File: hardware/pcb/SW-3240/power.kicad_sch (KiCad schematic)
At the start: 59 parts, among them SW1 PWR_SW, U10 LMR14050, U11 NCP1117-3.3, U8 TPS54231, U9 LM2941

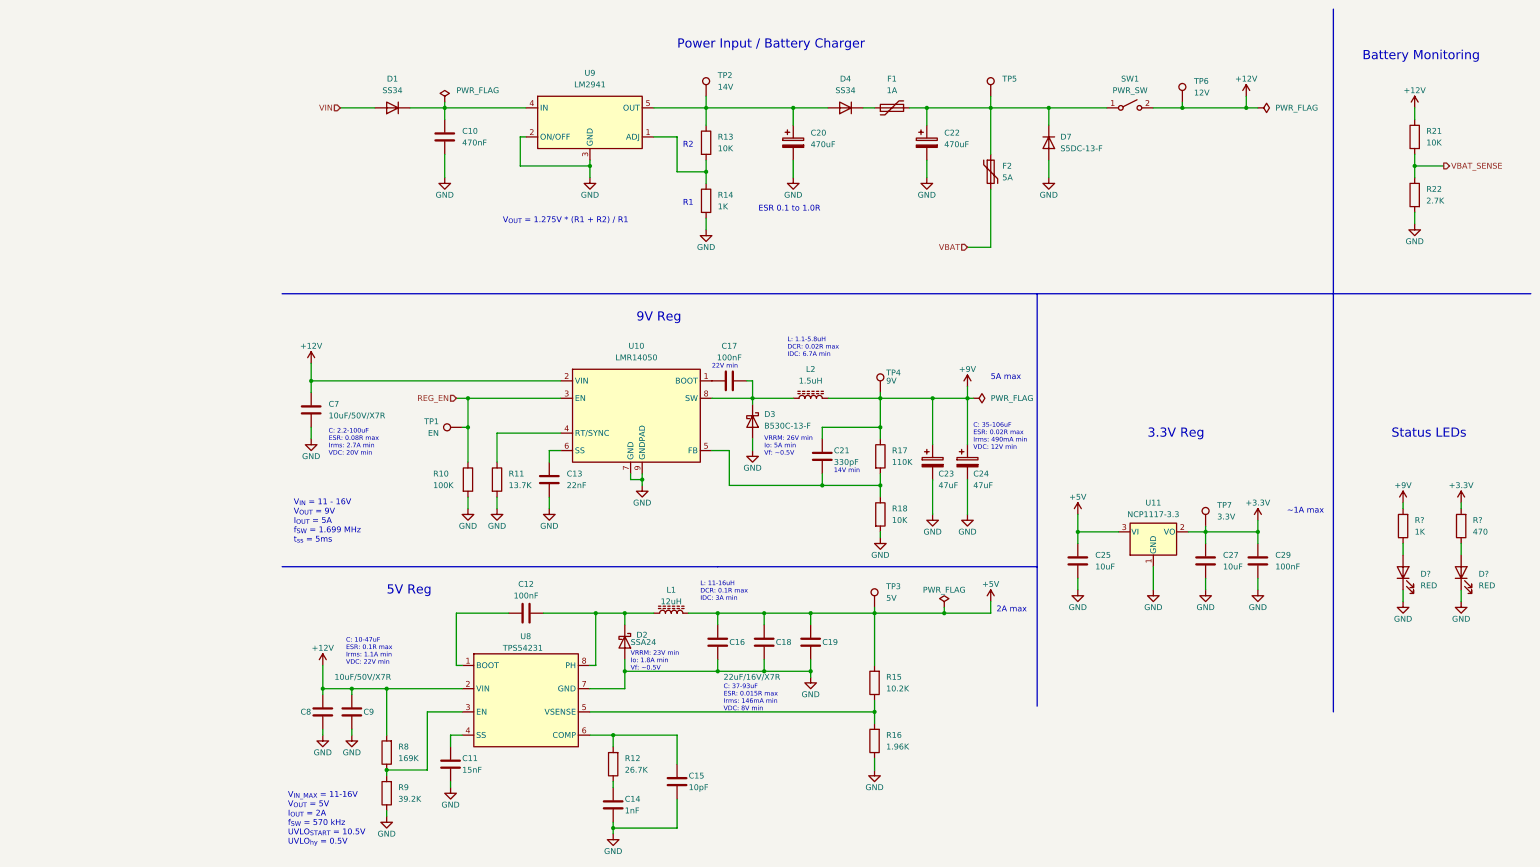
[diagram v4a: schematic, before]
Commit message: use atmega328pb for main board
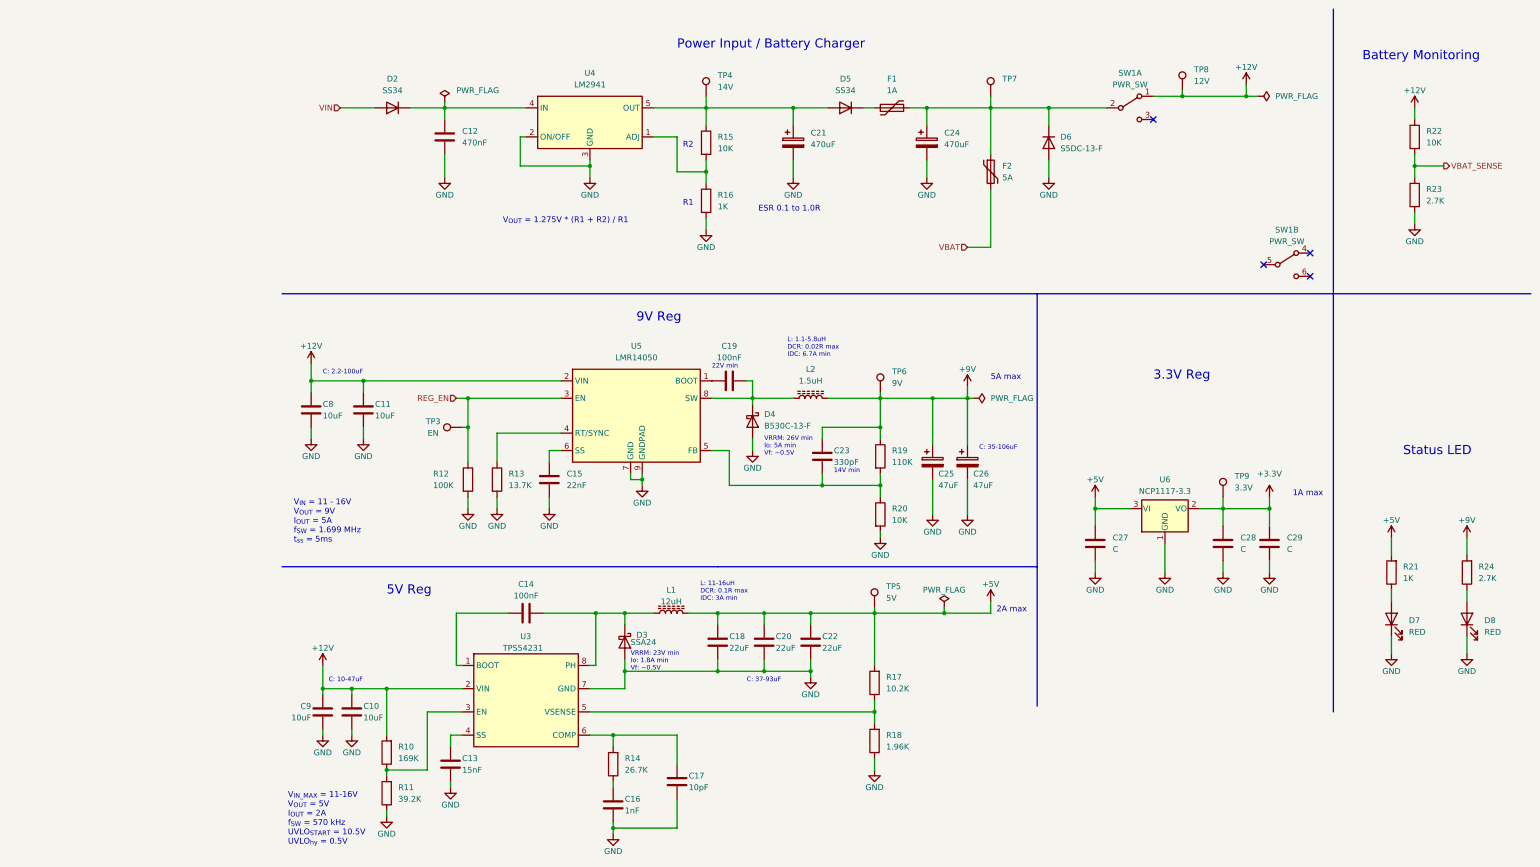
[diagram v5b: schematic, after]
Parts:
- removed C25: 10uF, Capacitor_SMD:C_0603_1608Metric, symbol Device:C
- removed D?: RED, LED_SMD:LED_0805_2012Metric, symbol Device:LED
- removed R?: 470, Resistor_SMD:R_0603_1608Metric, symbol Device:R
- removed SW1: PWR_SW, Button_Switch_THT:SW_E-Switch_EG2219_DPDT_Angled, symbol Switch:SW_SPST
- removed TP7: 3.3V, TestPoint:TestPoint_THTPad_D2.0mm_Drill1.0mm, symbol Connector:TestPoint
- removed U11: NCP1117-3.3, Package_TO_SOT_SMD:SOT-223-3_TabPin2, symbol Regulator_Linear:NCP1117-3.3_SOT223
- added C11: 10uF, Capacitor_SMD:C_1210_3225Metric, symbol Device:C
- added C28: C, Capacitor_SMD:C_0603_1608Metric, symbol Device:C
- added D7: RED, LED_SMD:LED_0603_1608Metric, symbol Device:LED
- added R21: 1K, Resistor_SMD:R_0603_1608Metric, symbol Device:R
- added SW1: PWR_SW, Button_Switch_THT:SW_E-Switch_EG2219_DPDT_Angled, symbol Switch:SW_DPDT_x2
- added TP9: 3.3V, TestPoint:TestPoint_Pad_D1.5mm, symbol Connector:TestPoint
- added U6: NCP1117-3.3, Package_TO_SOT_SMD:SOT-223-3_TabPin2, symbol Regulator_Linear:NCP1117-3.3_SOT223
- C10: renamed from C9; value 10uF/50V/X7R -> 10uF
- C18: renamed from C16; value 22uF/16V/X7R -> 22uF
- C20: renamed from C18; value 22uF/16V/X7R -> 22uF
- C22: renamed from C19; value 22uF/16V/X7R -> 22uF
- C25: renamed from C23; footprint Capacitor_SMD:CP_Elec_5x4.4 -> Capacitor_SMD:C_Elec_6.3x5.8; LCSC (none) -> C2162033; MOUSER (none) -> 710-875105445006; MPN 16SVPG47M -> 875105445006
- C26: renamed from C24; footprint Capacitor_SMD:CP_Elec_5x4.4 -> Capacitor_SMD:C_Elec_6.3x5.8; LCSC (none) -> C2162033; MOUSER (none) -> 710-875105445006; MPN 16SVPG47M -> 875105445006
- C27: value 10uF -> C
- C29: value 100nF -> C
- C8: renamed from C7; value 10uF/50V/X7R -> 10uF
- C9: renamed from C8; value 10uF/50V/X7R -> 10uF
- D3: renamed from D2; value SSA24 -> SSA24; LCSC (none) -> C463660; MOUSER (none) -> 512-SSA24
- D4: renamed from D3; footprint (none) -> Diode_SMD:D_SMC; LCSC (none) -> C110488; MOUSER (none) -> 621-B530C-13-F
- D8: renamed from D?; footprint LED_SMD:LED_0805_2012Metric -> LED_SMD:LED_0603_1608Metric
- F1, F2: footprint (none) -> Fuse:Fuse_BelFuse_0ZRE0016FF_L9.9mm_W3.8mm
- L1: footprint (none) -> Inductor_SMD:L_Bourns_SRR1260; LCSC (none) -> C2041771; MOUSER (none) -> 652-SRR1206-120ML; MPN SDR1307-120ML -> SRR1206-120ML
- L2: footprint (none) -> Inductor_SMD:L_Bourns-SRN8040_8x8.15mm; LCSC (none) -> C2041626; MOUSER (none) -> 652-SRN8040-1R5Y
- R24: renamed from R?; value 1K -> 2.7K
- TP3: renamed from TP1; footprint TestPoint:TestPoint_THTPad_D2.0mm_Drill1.0mm -> TestPoint:TestPoint_Pad_D1.5mm
- TP4: renamed from TP2; footprint TestPoint:TestPoint_THTPad_D2.0mm_Drill1.0mm -> TestPoint:TestPoint_Pad_D1.5mm
- TP5: renamed from TP3; footprint TestPoint:TestPoint_THTPad_D2.0mm_Drill1.0mm -> TestPoint:TestPoint_Pad_D1.5mm
- TP6: renamed from TP4; footprint TestPoint:TestPoint_THTPad_D2.0mm_Drill1.0mm -> TestPoint:TestPoint_Pad_D1.5mm
- TP7: renamed from TP5; footprint TestPoint:TestPoint_THTPad_D2.0mm_Drill1.0mm -> TestPoint:TestPoint_Pad_D1.5mm
- TP8: renamed from TP6; footprint TestPoint:TestPoint_THTPad_D2.0mm_Drill1.0mm -> TestPoint:TestPoint_Pad_D1.5mm
- U3: renamed from U8; LCSC (none) -> C28023; MOUSER (none) -> 595-TPS54231DR; MPN (none) -> TPS54231DR
- U4: renamed from U9; LCSC (none) -> C95046; MOUSER (none) -> 926-LM2941SX/NOPB; MPN (none) -> LM2941SX/NOPB
- U5: renamed from U10; LCSC (none) -> C155484; MOUSER (none) -> 595-LMR14050SDDAR; MPN (none) -> LMR14050SDDAR
- renumbered C10 to C12, C11 to C13, C12 to C14, C13 to C15, C14 to C16, C15 to C17, C17 to C19, C20 to C21, C21 to C23, C22 to C24, D1 to D2, D4 to D5, D7 to D6, R8 to R10, R9 to R11, R10 to R12, R11 to R13, R12 to R14, R13 to R15, R14 to R16, R15 to R17, R16 to R18, R17 to R19, R18 to R20, R21 to R22, R22 to R23
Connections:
- net +12V: now also C11.1, SW1.1 (A)
- net +3V3: now also C28.1, TP9.1, U6.2 (VO); no longer C27.1
- net +5V: now also C27.1, R21.2, U6.3 (VI)
- net GND: now also C11.2, C28.2, D7.1 (K), U6.1 (GND)
- net at C24.1, D6.1 (K), F1.2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: now also SW1.2 (B)
- new net: D7.2 (A), R21.1
- no-connect marks 0 -> 4
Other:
- note added: "1A max"
- note added: "C: 10-47uF"
- note added: "C: 2.2-100uF"
- note added: "C: 35-106uF"
- note added: "C: 37-93uF"
- note added: "Status LED"
- note removed: "C: 10-47uF ESR: 0.1R max Irms: 1.1A min VDC: 22V min"
- note removed: "C: 2.2-100uF ESR: 0.08R max Irms: 2.7A min VDC: 20V min"
- note removed: "C: 35-106uF ESR: 0.02R max Irms: 490mA min VDC: 12V min"
- note removed: "C: 37-93uF ESR: 0.015R max Irms: 146mA min VDC: 8V min"
- note removed: "Status LEDs"
- note removed: "~1A max"
- moved on the sheet: D8, R24, TP8

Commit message: major changes
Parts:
- removed C16: 1nF, Capacitor_SMD:C_0603_1608Metric, symbol Device:C
- removed C17: 10pF, Capacitor_SMD:C_0603_1608Metric, symbol Device:C
- removed C18, C20, C22: 22uF, Capacitor_SMD:C_1210_3225Metric, symbol Device:C
- removed C19: 100nF, Capacitor_SMD:C_0603_1608Metric, symbol Device:C
- removed C23: 330pF, Capacitor_SMD:C_0603_1608Metric, symbol Device:C
- removed C25, C26: 47uF, Capacitor_SMD:C_Elec_6.3x5.8, symbol Device:C_Polarized
- removed C8, C9: 10uF, Capacitor_SMD:C_1210_3225Metric, symbol Device:C
- removed D4: B530C-13-F, Diode_SMD:D_SMC, symbol Device:D_Schottky
- removed D6: S5DC-13-F, Diode_SMD:D_SMC, symbol Device:D
- removed L2: 1.5uH, Inductor_SMD:L_Bourns-SRN8040_8x8.15mm, symbol Device:L_Ferrite
- removed R10: 169K, Resistor_SMD:R_0603_1608Metric, symbol Device:R
- removed R11: 39.2K, Resistor_SMD:R_0603_1608Metric, symbol Device:R
- removed R19: 110K, Resistor_SMD:R_0603_1608Metric, symbol Device:R
- removed TP3: EN, TestPoint:TestPoint_Pad_D1.5mm, symbol Connector:TestPoint
- removed U3: TPS54231, Package_SO:SOIC-8_3.9x4.9mm_P1.27mm, symbol SaawLib:TPS54231
- removed U5: LMR14050, Package_SO:TI_SO-PowerPAD-8, symbol SaawLib:LMR14050
- added C12: 10uF, Capacitor_SMD:C_1210_3225Metric, symbol Device:C
- added C18: 180uF, Capacitor_SMD:CP_Elec_10x7.9, symbol Device:C_Polarized
- added C19: 330uF, Capacitor_SMD:CP_Elec_10x12.6, symbol Device:C_Polarized
- added C8, C9: 100uF, Capacitor_THT:C_Radial_D8.0mm_H11.5mm_P3.50mm, symbol Device:C_Polarized
- added D3: SSB44-E3, Diode_SMD:D_SMB, symbol Device:D_Schottky
- added L1: 15uH, Inductor_SMD:L_Bourns_SRR1260, symbol Device:L_Ferrite
- added U3, U4: TPS5430DDA, Package_SO:TI_SO-PowerPAD-8_ThermalVias, symbol Regulator_Switching:TPS5430DDA
- C10, C11: LCSC (none) -> C66120; MOUSER (none) -> 187-CL32A106KAJNNNE; MPN (none) -> CL32A106KAJNNNE
- C13: value 15nF -> 10uF; footprint Capacitor_SMD:C_0603_1608Metric -> Capacitor_SMD:C_1210_3225Metric; LCSC (none) -> C66120; MOUSER (none) -> 187-CL32A106KAJNNNE; MPN (none) -> CL32A106KAJNNNE
- C14: renamed from C12; LCSC (none) -> C170149; MOUSER (none) -> 187-CL10A474KB8NNNC; MPN (none) -> CL10A474KB8NNNC
- C15: value 22nF -> 10nF; LCSC (none) -> C1589; MOUSER (none) -> 187-CL10B103KB8NNNC; MPN (none) -> CL10B103KB8NNNC
- C16: renamed from C14; value 100nF -> 10nF; LCSC (none) -> C1589; MOUSER (none) -> 187-CL10B103KB8NNNC; MPN (none) -> CL10B103KB8NNNC
- C17: renamed from C21; value 470uF -> 100uF
- C20: renamed from C24; value 470uF -> 330uF
- C21: renamed from C27; value C -> 10uF; LCSC (none) -> C2922482; MOUSER (none) -> 187-CL10A106MA8NRNC; MPN (none) -> CL10A106MA8NRNC
- C22: renamed from C28; value C -> 10uF; LCSC (none) -> C2922482; MOUSER (none) -> 187-CL10A106MA8NRNC; MPN (none) -> CL10A106MA8NRNC
- C23: renamed from C29; value C -> 100nF; LCSC (none) -> C1591; MOUSER (none) -> 187-CL10B104KB8NNNC; MPN (none) -> CL10B104KB8NNNC
- D2, D5: value SS34 -> SSB44-E3; footprint Diode_SMD:D_SMC -> Diode_SMD:D_SMB; symbol Device:D -> Device:D_Schottky; LCSC (none) -> C466999; MOUSER (none) -> 625-SSB44-E3; MPN (none) -> SSB44-E3/52T
- D4: renamed from D3; value SSA24 -> SSB44-E3; footprint Diode_SMD:D_SMA -> Diode_SMD:D_SMB; LCSC C463660 -> C466999; MOUSER 512-SSA24 -> 625-SSB44-E3; MPN SSA24 -> SSB44-E3/52T
- D6: renamed from D7; value RED -> GREEN; MOUSER (none) -> 710-150060VS75000; MPN (none) -> 150060VS75000
- D7: renamed from D8; value RED -> BLUE; MOUSER (none) -> 710-150060BS75000; MPN (none) -> 150060BS75000
- F1: footprint Fuse:Fuse_BelFuse_0ZRE0016FF_L9.9mm_W3.8mm -> Fuse:Fuse_BelFuse_0ZRE0005FF_L8.3mm_W3.8mm; LCSC (none) -> C207122; MOUSER (none) -> 576-72R050XPR; MPN (none) -> 72R050XPR
- F2: value 5A -> 4A; LCSC (none) -> C142903; MPN (none) -> RF3357-000
- L2: renamed from L1; value 12uH -> 15uH; LCSC C2041771 -> C2041333; MOUSER 652-SRR1206-120ML -> 652-SRR1260-150M; MPN SRR1206-120ML -> SRR1260-150M
- R10: renamed from R12; LCSC (none) -> C14675; MOUSER (none) -> 603-RC0603FR-07100KL; MPN (none) -> RC0603FR-07100KL
- R11: renamed from R15; LCSC (none) -> C98220; MOUSER (none) -> 603-RC0603FR-0710KL; MPN (none) -> RC0603FR-0710KL
- R12: renamed from R16; LCSC (none) -> C22548; MOUSER (none) -> 603-RC0603FR-071KL; MPN (none) -> RC0603FR-071KL
- R13: value 13.7K -> 10K; LCSC (none) -> C98220; MOUSER (none) -> 603-RC0603FR-0710KL; MPN (none) -> RC0603FR-0710KL
- R14: value 26.7K -> 1.5K; LCSC (none) -> C114668; MOUSER (none) -> 603-RC0603FR-071K5L; MPN (none) -> RC0603FR-071K5L
- R15: renamed from R17; value 10.2K -> 10K; LCSC (none) -> C98220; MOUSER (none) -> 603-RC0603FR-0710KL; MPN (none) -> RC0603FR-0710KL
- R16: renamed from R18; value 1.96K -> 3.24K; LCSC (none) -> C273779; MOUSER (none) -> 603-RC0603FR-073K24L; MPN (none) -> RC0603FR-073K24L
- R17: renamed from R21; LCSC (none) -> C22548; MOUSER (none) -> 603-RC0603FR-071KL; MPN (none) -> RC0603FR-071KL
- R18: renamed from R22; LCSC (none) -> C98220; MOUSER (none) -> 603-RC0603FR-0710KL; MPN (none) -> RC0603FR-0710KL
- R19: renamed from R23; value 2.7K -> 4.7K; LCSC (none) -> C99782; MOUSER (none) -> 603-RC0603FR-074K7L; MPN (none) -> RC0603FR-074K7L
- R20: value 10K -> 1K; LCSC (none) -> C22548; MOUSER (none) -> 603-RC0603FR-071KL; MPN (none) -> RC0603FR-071KL
- R21: renamed from R24; value 2.7K -> 1K; LCSC (none) -> C22548; MOUSER (none) -> 603-RC0603FR-071KL; MPN (none) -> RC0603FR-071KL
- SW1: MOUSER (none) -> 612-EG2219; MPN (none) -> EG2219
- TP2: renamed from TP4; now left out of the parts list
- TP3: renamed from TP6; value 9V -> 9.2V; now left out of the parts list
- TP4: renamed from TP5; now left out of the parts list
- TP5: renamed from TP7; value 13.5V -> VBAT; now left out of the parts list
- TP6: renamed from TP8; now left out of the parts list
- TP7: renamed from TP9; now left out of the parts list
- U6: LCSC (none) -> C146799; MOUSER (none) -> 863-NCP1117LPST33T3G; MPN (none) -> NCP1117LPST33T3G
- renumbered U4 to U5
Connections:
- net +12V: now also C11.2, C13.2, C12.2, C8.1, C9.1, U3.7 (VIN), U4.7 (VIN); no longer C11.1
- net +5V: now also C19.1
- net +9V: now also R13.2, R20.2, C18.1, L1.2; no longer R21.2
- net GND: now also C11.1, R14.1, C12.1, C18.2, C19.2, C8.2, C9.2, D3.2 (A), U3.6 (GND), U3.9 (GNDPAD), U4.6 (GND), U4.9 (GNDPAD); no longer C11.2, C15.1, R13.2, R20.2
- net REG_EN: now also U3.5 (EN)
- net at R20.1: now also R21.2
- net at C15.2: now also D3.1 (K), L1.1, U3.8 (PH)
- net at R15.1, R16.2: now also U4.4 (VSENSE)
- net at R13.1: now also R14.2, U3.4 (VSENSE)
- net at C16.2, D4.1 (K), L2.1: now also U4.8 (PH)
- net at C16.1: now also U4.1 (BOOT)
- new net: C15.1, U3.1 (BOOT)
- no-connect marks 4 -> 5
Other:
- note added: "3A max"
- note added: "Cout - C: 120 μF - 190 μF ESR: 35 mΩ - 75 mΩ"
- note added: "Cout - C: 280 μF - 425 μF ESR: 15 mΩ - 35 mΩ"
- note added: "TODO: Check charger caps values / footprints Check regulator bulk caps footprints"
- note added: "VRRM: 23V IOmin: 1.75A"
- note added: "VRRM: 23V IOmin: 2.75A"
- note added: "V_{OUT} = 1.275V * ((R1 + R2) / R1)"
- note added: "Vf: ~2.1V"
- note added: "Vf: ~3.6V"
- note added: "Vin = 10.9-16.0V Vout = 5V Iout = 3A f = 500kHz Vout p-p = max. 8mv"
- note added: "Vin = 10.9-16.0V Vout = 9V Iout = 3A f = 500kHz Vout p-p = max. 15mv"
- note removed: "14V min"
- note removed: "22V min"
- note removed: "2A max"
- note removed: "5A max"
- note removed: "C: 10-47uF"
- note removed: "C: 2.2-100uF"
- note removed: "C: 35-106uF"
- note removed: "C: 37-93uF"
- note removed: "L: 1.1-5.8uH DCR: 0.02R max IDC: 6.7A min"
- note removed: "L: 11-16uH DCR: 0.1R max IDC: 3A min"
- note removed: "VRRM: 23V min Io: 1.8A min Vf: ~0.5V"
- note removed: "VRRM: 26V min Io: 5A min Vf: ~0.5V"
- note removed: "V_{IN_MAX} = 11-16V V_{OUT} = 5V I_{OUT} = 2A f_{SW} = 570 kHz UVLO_{START} = 10.5V UVLO_{hy} = 0.5V"
- note removed: "V_{IN} = 11 - 16V V_{OUT} = 9V I_{OUT} = 5A f_{SW} = 1.699 MHz t_{ss} = 5ms"
- note removed: "V_{OUT} = 1.275V * (R1 + R2) / R1"
- moved on the sheet: C16, C20, C23, D4, D6, D7, F1, F2, L2, R10, R15, R16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
